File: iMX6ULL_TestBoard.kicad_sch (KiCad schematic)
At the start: 1 part, among them J1 USB_B_Mini

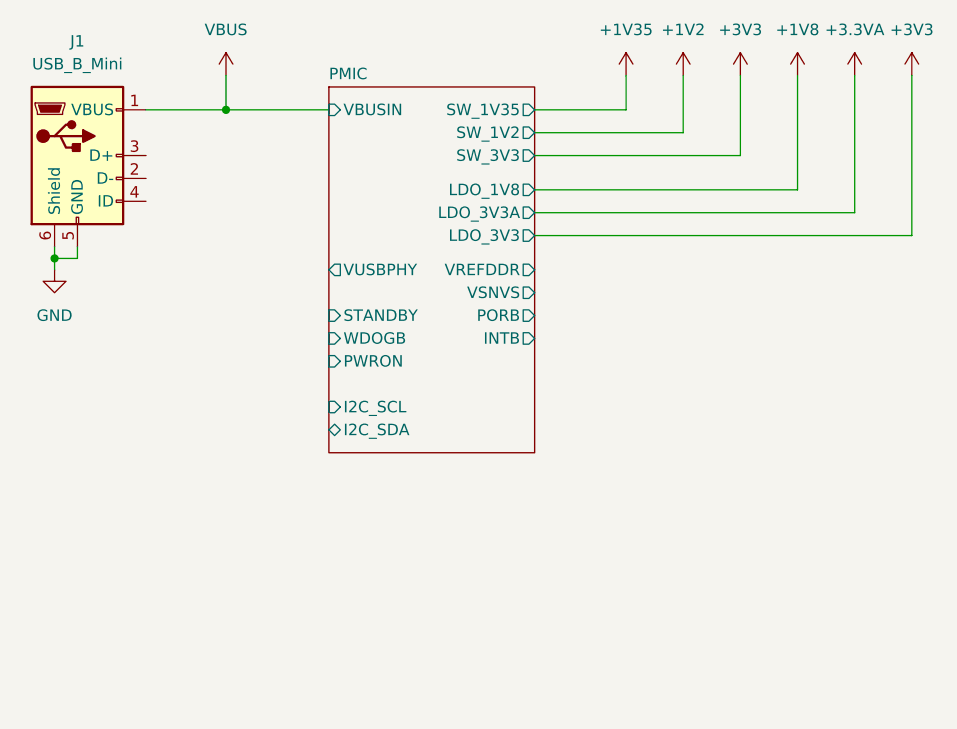
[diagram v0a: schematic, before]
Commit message: Added IMX6ULL Power, Control and DDR sheets. Added symbol library with used custom components.
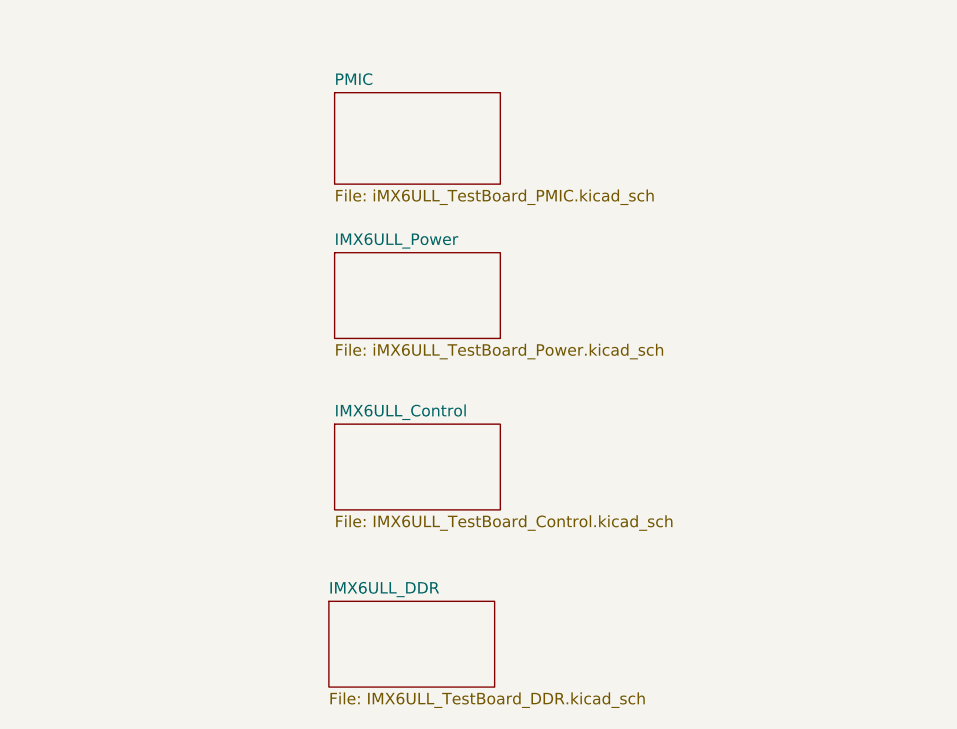
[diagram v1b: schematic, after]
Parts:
- removed J1: USB_B_Mini, symbol Connector:USB_B_Mini
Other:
- added sheet IMX6ULL_Control (IMX6ULL_TestBoard_Control.kicad_sch)
- added sheet IMX6ULL_DDR (IMX6ULL_TestBoard_DDR.kicad_sch)
- added sheet IMX6ULL_Power (iMX6ULL_TestBoard_Power.kicad_sch)
- sheet PMIC ports: added none; removed I2C_SCL, I2C_SDA, INTB, LDO_1V8, LDO_3V3, LDO_3V3A, PORB, PWRON, STANDBY, SW_1V2, SW_1V35, SW_3V3, VBUSIN, VREFDDR, VSNVS, VUSBPHY, WDOGB
